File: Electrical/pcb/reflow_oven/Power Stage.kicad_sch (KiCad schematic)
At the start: 29 parts, among them J1 1711738, J14 3V3 out, J15 5V out, U1 LH05-10B05, U2 AP1117-33

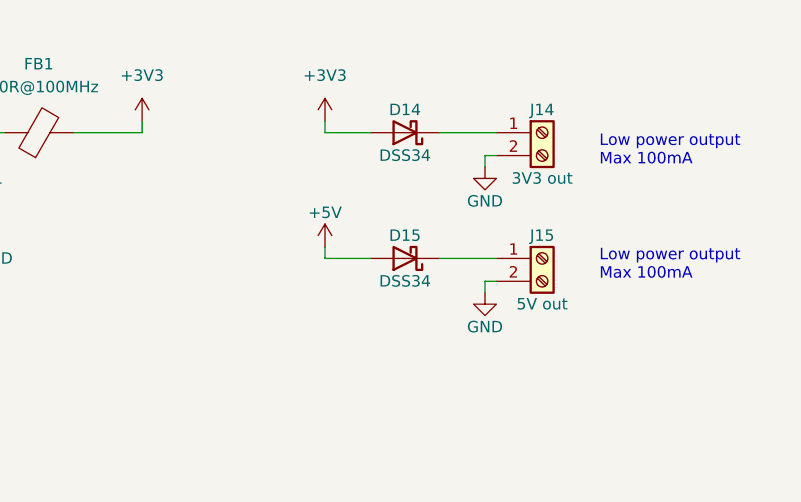
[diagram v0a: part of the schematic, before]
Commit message: addon
documentation pics
adjust oshw logo
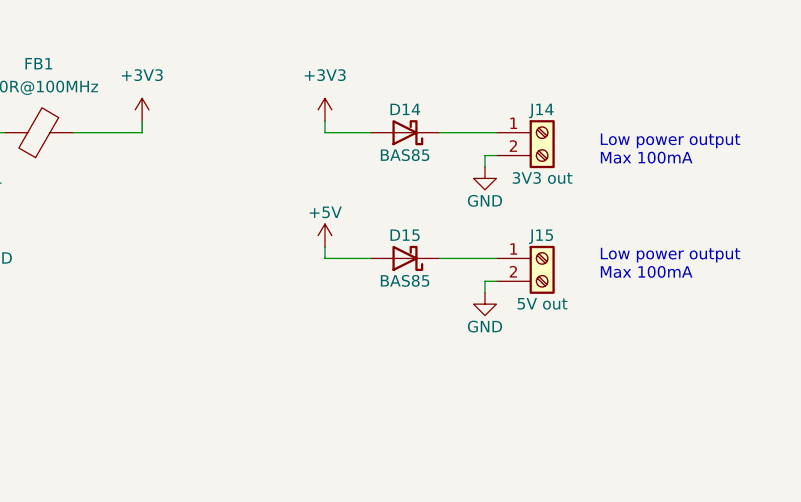
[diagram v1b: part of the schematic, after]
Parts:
- D14, D15: value DSS34 -> BAS85
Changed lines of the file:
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@@
     (in_bom yes) (on_board yes)
     (property "Reference" "D14" (id 0) (at 229.87 53.34 0))
-    (property "Value" "DSS34" (id 1) (at 229.87 58.42 0))
+    (property "Value" "BAS85" (id 1) (at 229.87 58.42 0))
     (property "Footprint" "Diode_SMD:D_SOD-123F" (id 2) (at 229.87 55.88 0)
       (effects (font (size 1.27 1.27)) hide)
@@
     (in_bom yes) (on_board yes)
     (property "Reference" "D15" (id 0) (at 229.87 67.31 0))
-    (property "Value" "DSS34" (id 1) (at 229.87 72.39 0))
+    (property "Value" "BAS85" (id 1) (at 229.87 72.39 0))
     (property "Footprint" "Diode_SMD:D_SOD-123F" (id 2) (at 229.87 69.85 0)
       (effects (font (size 1.27 1.27)) hide)
